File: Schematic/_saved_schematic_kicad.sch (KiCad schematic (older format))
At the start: 249 parts

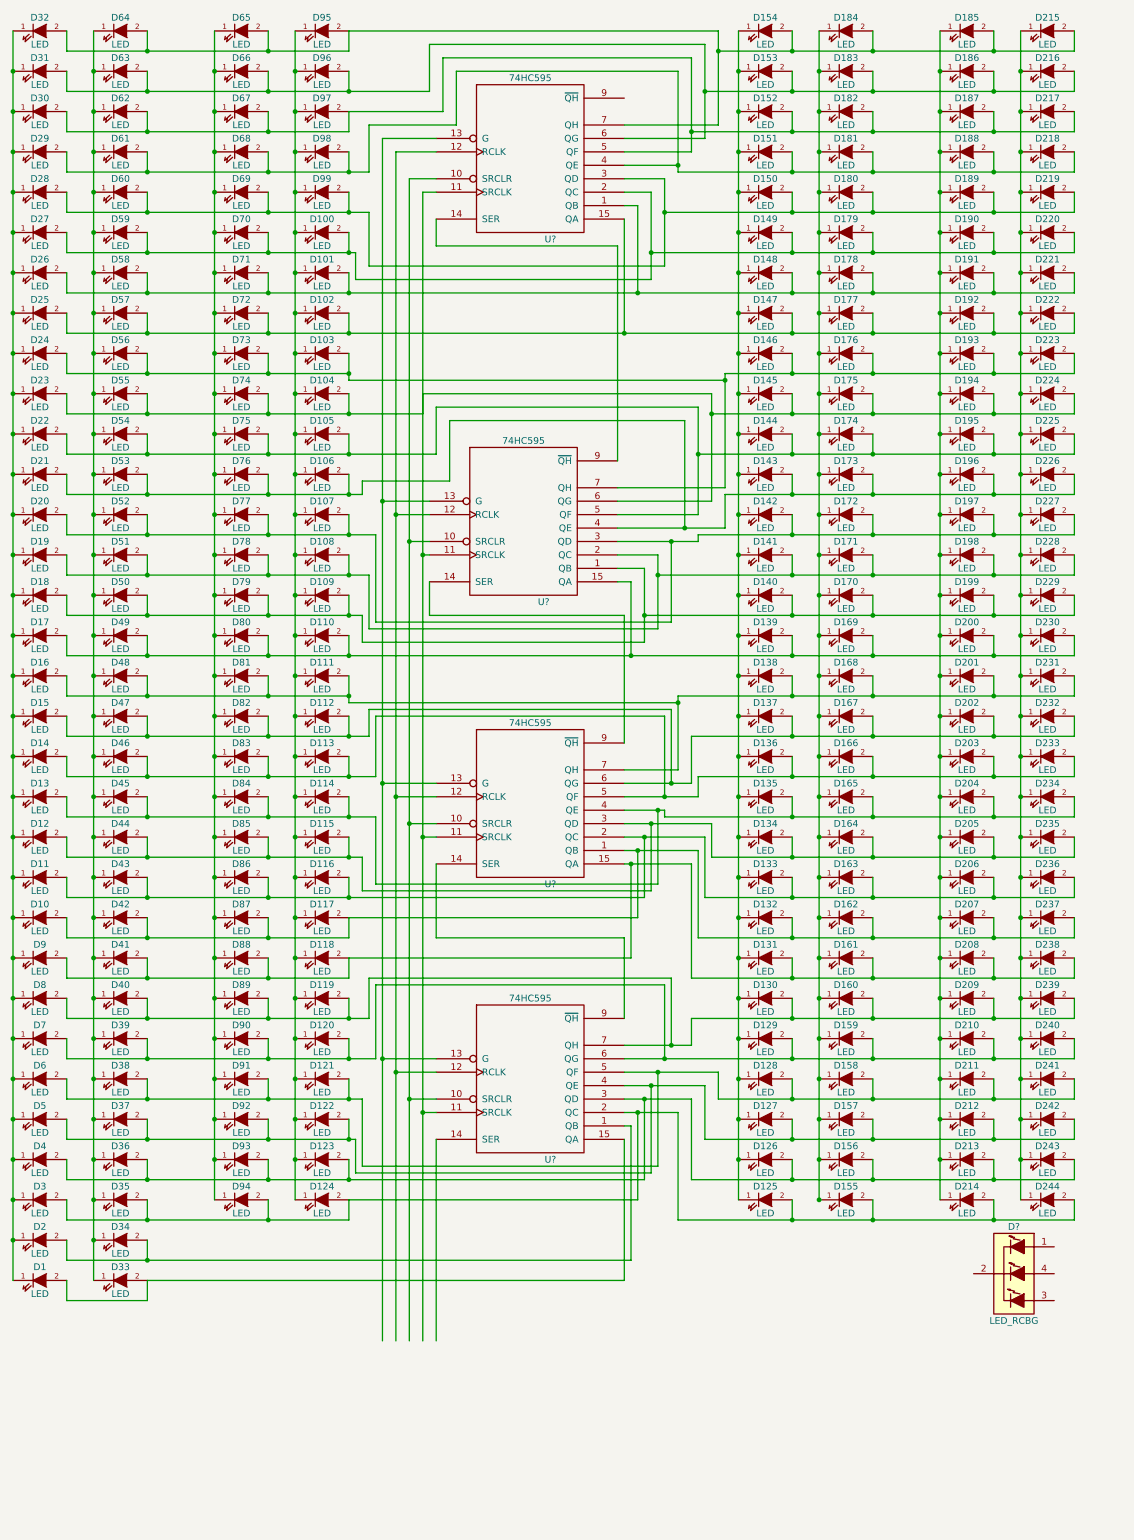
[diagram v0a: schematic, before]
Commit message: Rearranged LEDs
LEDs were moved to reflect changes in plans for the physical board
layout. This change will make it easier to wire it to the shift
registers.
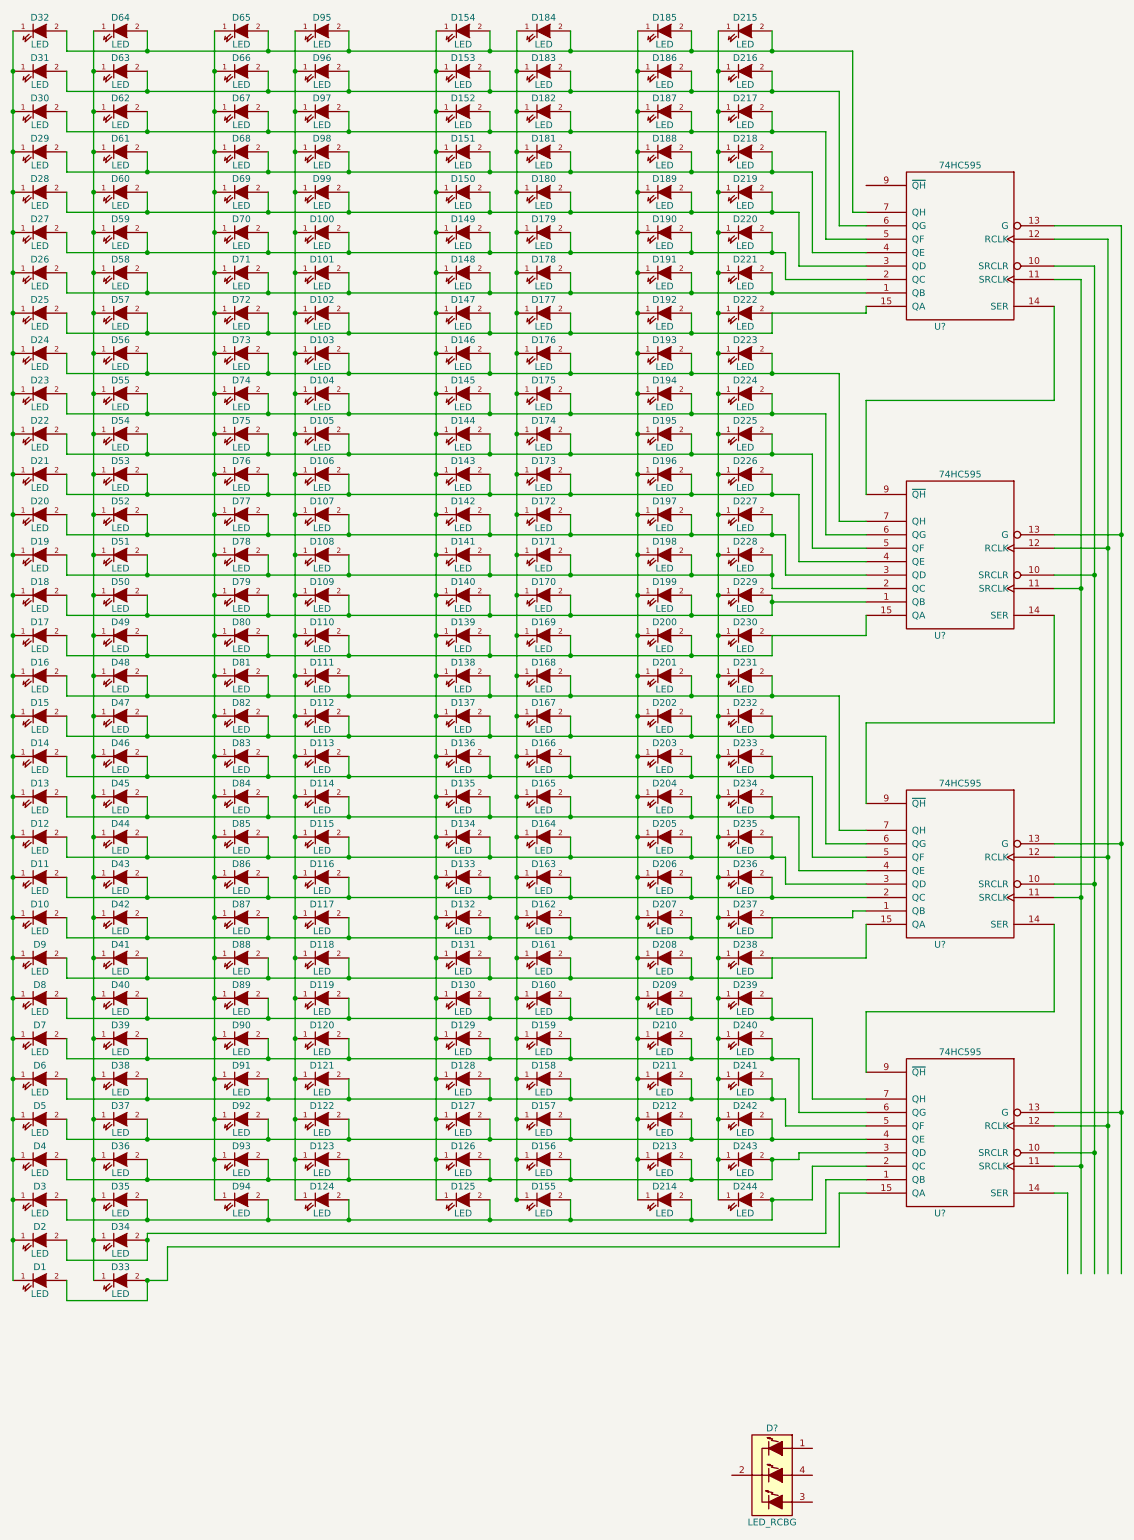
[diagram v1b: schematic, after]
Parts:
- removed U? (x2): 74HC595, symbol 74HC595
- added U? (x2): 74HC595, symbol 74HC595
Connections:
- net GND: now also U?.8 (GND), U?.8 (GND)
- net VCC: now also U?.16 (VCC), U?.16 (VCC)
- net at D154.2 (A), D184.2 (A), D185.2 (A)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: now also U?.7 (QH)
- net at D153.2 (A), D183.2 (A), D186.2 (A)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: now also U?.6 (QG)
- net at D152.2 (A), D182.2 (A), D187.2 (A)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: now also U?.5 (QF)
- net at D151.2 (A), D181.2 (A), D188.2 (A)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: now also U?.4 (QE)
- net at D150.2 (A), D180.2 (A), D189.2 (A)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: now also U?.3 (QD)
- net at D100.2 (A), D149.2 (A), D179.2 (A)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: now also U?.2 (QC)
- net at D101.2 (A), D148.2 (A), D178.2 (A)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: now also U?.1 (QB)
- net at D102.2 (A), D147.2 (A), D177.2 (A)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: now also U?.15 (QA)
- net at D103.2 (A), D146.2 (A), D176.2 (A)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: now also U?.7 (QH); no longer U?.7 (QH)
- net at D104.2 (A), D145.2 (A), D175.2 (A)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: now also U?.6 (QG); no longer U?.11 (SRCLK), U?.11 (SRCLK), U?.6 (QG)
- net at D105.2 (A), D144.2 (A), D174.2 (A)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: now also U?.5 (QF); no longer U?.5 (QF)
- net at D106.2 (A), D143.2 (A), D173.2 (A)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: now also U?.4 (QE); no longer U?.4 (QE)
- net at D107.2 (A), D142.2 (A), D172.2 (A)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: now also U?.3 (QD); no longer U?.3 (QD)
- net at D108.2 (A), D141.2 (A), D171.2 (A)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: now also U?.2 (QC); no longer U?.2 (QC)
- net at D109.2 (A), D140.2 (A), D170.2 (A)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: now also U?.1 (QB); no longer U?.1 (QB)
- net at D110.2 (A), D139.2 (A), D169.2 (A)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: now also U?.15 (QA); no longer U?.15 (QA)
- net at D111.2 (A), D138.2 (A), D16.2 (A)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: now also U?.7 (QH); no longer U?.7 (QH)
- net at D112.2 (A), D137.2 (A), D15.2 (A)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: now also U?.6 (QG); no longer U?.6 (QG)
- net at D113.2 (A), D136.2 (A), D14.2 (A)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: now also U?.5 (QF); no longer U?.5 (QF)
- net at D114.2 (A), D13.2 (A), D135.2 (A)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: now also U?.4 (QE); no longer U?.4 (QE)
- net at D115.2 (A), D12.2 (A), D134.2 (A)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: now also U?.3 (QD); no longer U?.3 (QD)
- net at D11.2 (A), D116.2 (A), D133.2 (A)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: now also U?.2 (QC); no longer U?.2 (QC)
- net at D10.2 (A), D117.2 (A), D132.2 (A)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: now also U?.1 (QB); no longer U?.1 (QB)
- net at D118.2 (A), D131.2 (A), D161.2 (A)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: now also U?.15 (QA); no longer U?.15 (QA)
- net at D119.2 (A), D130.2 (A), D160.2 (A)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: now also U?.7 (QH)
- net at D120.2 (A), D129.2 (A), D159.2 (A)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: now also U?.6 (QG)
- net at D121.2 (A), D128.2 (A), D158.2 (A)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: now also U?.5 (QF)
- net at D122.2 (A), D127.2 (A), D157.2 (A)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: now also U?.4 (QE)
- net at D123.2 (A), D126.2 (A), D156.2 (A)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: now also U?.3 (QD)
- net at D124.2 (A), D125.2 (A), D155.2 (A)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: now also U?.2 (QC)
- net at D2.2 (A), D34.2 (A): now also U?.1 (QB)
- net at D1.2 (A), D33.2 (A): now also U?.15 (QA)
- net at U?.10 (SRCLR), U?.10 (SRCLR): now also U?.10 (SRCLR), U?.10 (SRCLR)
- net at U?.12 (RCLK), U?.12 (RCLK): now also U?.12 (RCLK), U?.12 (RCLK)
- net at U?.13 (G), U?.13 (G): now also U?.13 (G), U?.13 (G)
- net at U?.14 (SER): now also U?.9 (~QH)
- new net: U?.11 (SRCLK), U?.11 (SRCLK), U?.11 (SRCLK), U?.11 (SRCLK)
- new net: U?.14 (SER), U?.9 (~QH)
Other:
- moved on the sheet: D125, D126, D127, D128, D129, D130, D131, D132, D133, D134, D135, D136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
